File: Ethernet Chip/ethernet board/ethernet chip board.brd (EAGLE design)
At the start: 102.5 x 80 mm, 33 parts

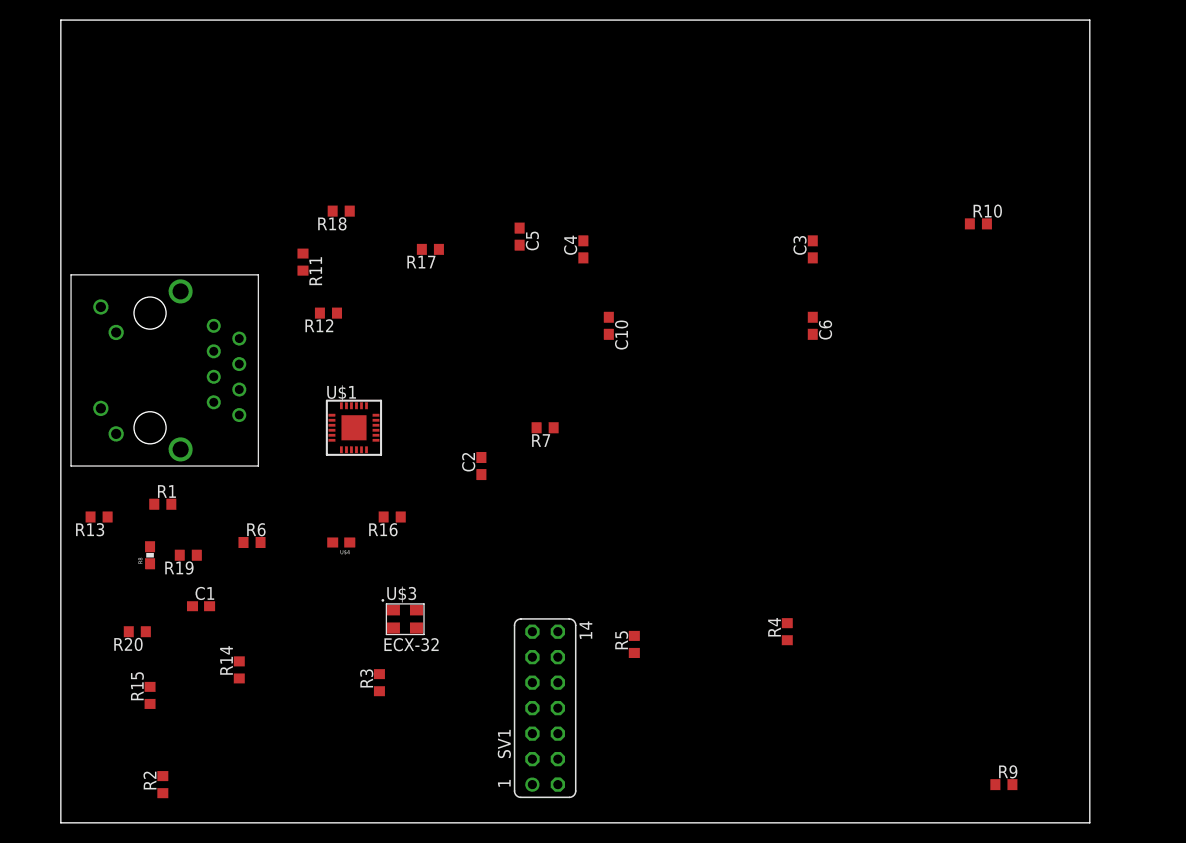
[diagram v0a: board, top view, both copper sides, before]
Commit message: Worked on the board layout for the ethernet circuit
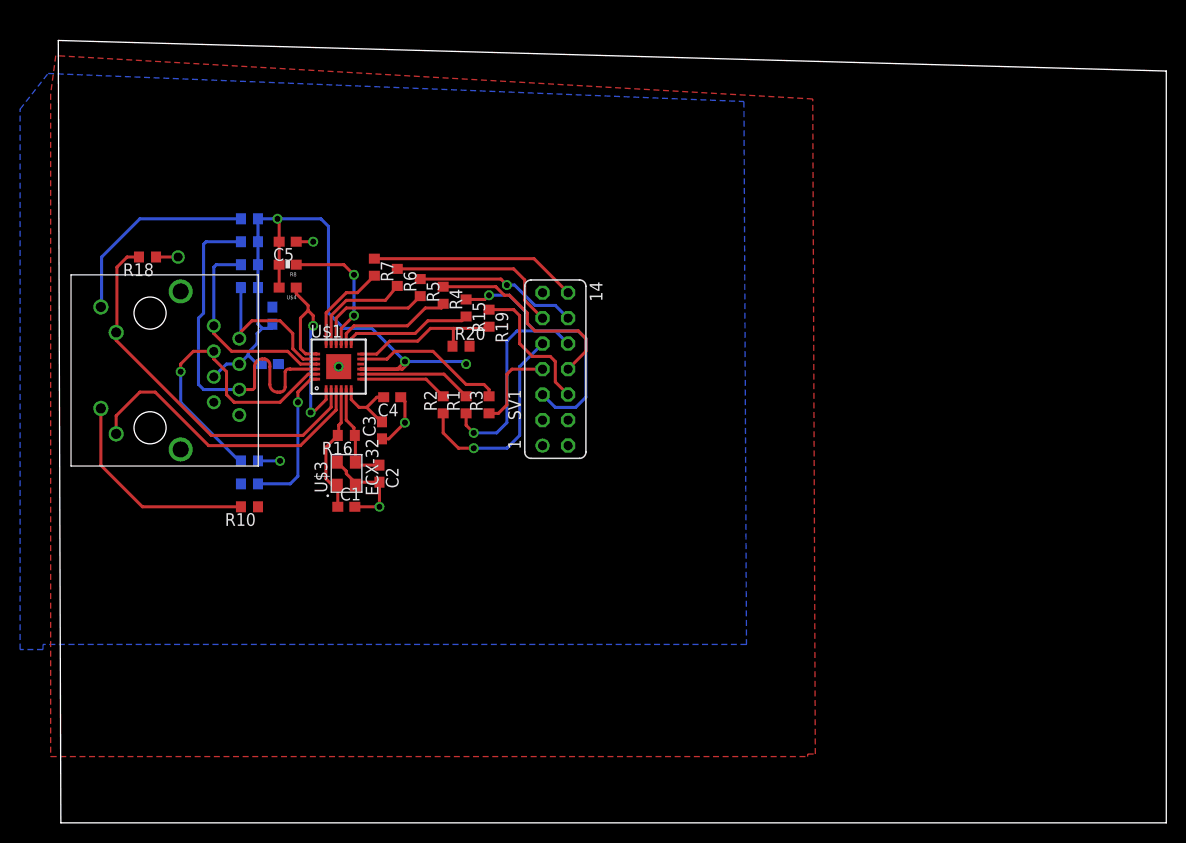
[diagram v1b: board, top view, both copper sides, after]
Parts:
- removed FRAME1: FRAME-LETTER, SparkFun-Aesthetics:CREATIVE_COMMONS
- R18: value 10K -> 4.7K
- moved R9 94.0 mm to (18.8, 60.2), flipped to the bottom
- moved R10 77.9 mm to (18.8, 31.5), turned to 180 degrees
- moved C6 54.2 mm to (20.8, 45.7), flipped to the bottom, turned to 0 degrees
- moved R15 49.8 mm to (40.4, 51.3), turned to 270 degrees
- moved R4 48.0 mm to (38.1, 52.6), turned to 270 degrees
- moved R2 47.0 mm to (38.1, 41.7)
- moved C3 46.6 mm to (32.0, 39.1)
- moved R20 43.0 mm to (39.9, 47.5), turned to 0 degrees
- moved R5 41.5 mm to (35.8, 53.3), turned to 270 degrees
- moved R14 40.4 mm to (18.8, 55.6), flipped to the bottom, turned to 180 degrees
- moved R19 38.2 mm to (42.7, 50.3), turned to 270 degrees
- moved SV1 33.8 mm to (49.3, 45.2)
- moved C10 33.5 mm to (21.1, 50.5), flipped to the bottom
- moved R8 32.0 mm to (22.6, 55.6), turned to 180 degrees
- moved R1 31.8 mm to (40.4, 41.7), turned to 90 degrees
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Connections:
- removed net RXDO: R1.1
- net RXD0: now also R1.1
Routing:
- net +3V3: track 0.00 -> 72.7 mm, vias 0 -> 4
- net BUS_SPEED: track 0.00 -> 38.3 mm
- net RD-: track 0.00 -> 36.7 mm
- net RD+: track 0.00 -> 31.4 mm, vias 0 -> 1
- net LINK/ACT: track 0.00 -> 30.5 mm
- net MDC: track 0.00 -> 25.6 mm, vias 0 -> 1
- net N$11: track 0.00 -> 22.4 mm, vias 0 -> 2
- net YELLOW: track 0.00 -> 21.3 mm
- net RXD0: track 0.00 -> 21.2 mm, vias 0 -> 1
- net TD+: track 0.00 -> 20.9 mm
- net RXD1: track 0.00 -> 20.8 mm, vias 0 -> 1
- net REFCLK: track 0.00 -> 20.7 mm
- net TXD1: track 0.00 -> 20.7 mm
- net GREEN: track 0.00 -> 20.5 mm
- net GND: track 0.00 -> 20.5 mm, vias 0 -> 5
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- added copper zone on layer 1, net +3V3
- added copper zone on layer 16, net GND
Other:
- board size 102.5 x 80 mm -> 110.4 x 78 mm

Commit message: updated the ethernet board
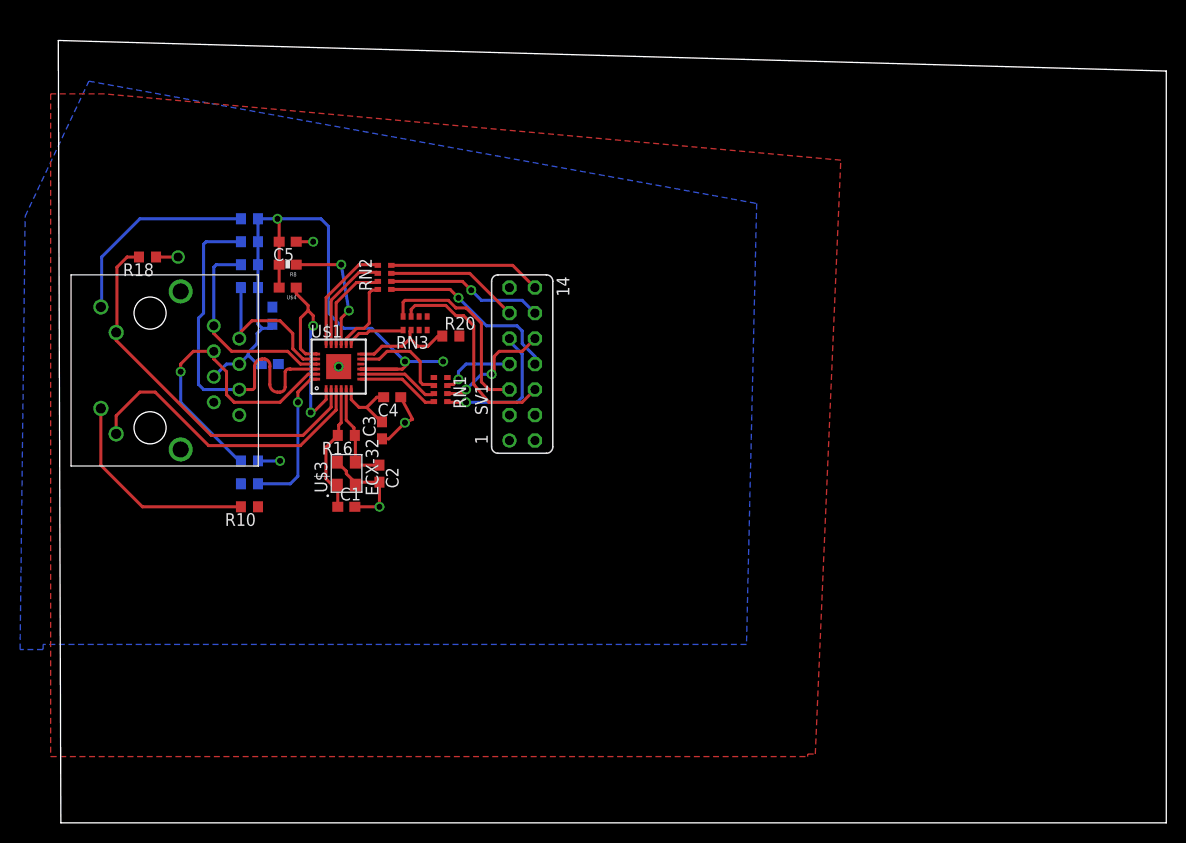
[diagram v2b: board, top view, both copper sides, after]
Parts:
- removed R1, R15, R19, R2, R3, R4, R5, R6, R7: 27R, resistor:R0603
- added RN1, RN2, RN3: (no value), resistor-dil:CAY16
- moved SV1 3.34 mm to (46.0, 45.7)
- moved R20 1.44 mm to (38.9, 48.5)
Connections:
- net CRS_DV: now also RN1.3; no longer R3.1
- net MDC: now also RN3.8; no longer R15.1
- net MDE: now also RN3.1; no longer R15.2
- net MDIO: now also RN3.7; no longer R19.1
- net N$1: now also RN1.7; no longer R1.2
- net N$10: now also RN2.1; no longer R7.2
- net N$12: now also RN3.2; no longer R19.2
- net N$2: now also RN1.8; no longer R2.2
- net N$5: now also RN1.6; no longer R3.2
- net N$7: now also RN2.4; no longer R4.2
- net N$8: now also RN2.3; no longer R5.2
- net N$9: now also RN2.2; no longer R6.2
- net REFCLK: now also RN2.5; no longer R4.1
- net RXD0: now also RN1.2; no longer R1.1
- net RXD1: now also RN1.1; no longer R2.1
- net TXD0: now also RN2.7; no longer R6.1
- net TXD1: now also RN2.8; no longer R7.1
- net TXEN: now also RN2.6; no longer R5.1
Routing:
- net RXD0: track 21.2 -> 11.9 mm, vias 1 -> 2
- net MDIO: track 14.2 -> 21.2 mm
- net MDE: track 12.9 -> 5.96 mm
- net RXD1: track 20.8 -> 14.1 mm
- net MDC: track 25.6 -> 19.2 mm, vias 1 -> 0
- net TXD1: track 20.7 -> 15.2 mm
- net N$12: track 15.8 -> 10.4 mm
- net N$5: track 15.4 -> 10.2 mm
- net N$7: track 12.1 -> 7.55 mm
- net TXD0: track 17.7 -> 13.4 mm
- net +3V3: track 72.7 -> 69.3 mm
- net N$1: track 11.4 -> 8.18 mm
- net N$8: track 11.9 -> 9.19 mm
- net REFCLK: track 20.7 -> 18.6 mm, vias 0 -> 1
- net N$10: track 9.50 -> 11.2 mm
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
